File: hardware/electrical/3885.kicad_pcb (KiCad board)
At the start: 4 copper layers, 33 x 77 mm, 9 parts, among them J1 USB_B_Micro, J4 JST-PH, J5 FFC, SW2 EVQP7C01K

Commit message: Component placement
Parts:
- added C1: 10u, Capacitor_SMD:C_0402_1005Metric, F.Cu at (146.7, 137.5)
- added C10: 100n, Capacitor_SMD:C_0402_1005Metric, F.Cu at (141.0, 116.0)
- added C11: 12p, Capacitor_SMD:C_0603_1608Metric, F.Cu at (137.8, 116.5)
- added C12: 100n, Capacitor_SMD:C_0402_1005Metric, F.Cu at (141.0, 120.0)
- added C13: 100n, Capacitor_SMD:C_0402_1005Metric, F.Cu at (146.0, 127.0)
- added C14: 12p, Capacitor_SMD:C_0603_1608Metric, F.Cu at (137.8, 119.5)
- added C15: 100n, Capacitor_SMD:C_0402_1005Metric, F.Cu at (156.8, 127.0)
- added C16: 100n, Capacitor_SMD:C_0402_1005Metric, F.Cu at (161.0, 111.0)
- added C17: 100n, Capacitor_SMD:C_0402_1005Metric, F.Cu at (145.0, 106.5)
- added C18: 100n, Capacitor_SMD:C_0402_1005Metric, F.Cu at (141.0, 114.9)
- added C2: 100n, Capacitor_SMD:C_0402_1005Metric, F.Cu at (140.8, 137.8)
- added C20: 2u2, Capacitor_SMD:C_0402_1005Metric, F.Cu at (155.5, 127.0)
- added C22: 2u2, Capacitor_SMD:C_0402_1005Metric, F.Cu at (161.0, 112.0)
- added C25: 4u7, Capacitor_SMD:C_0402_1005Metric, F.Cu at (141.0, 109.8)
- added C27: 100n, Capacitor_SMD:C_0402_1005Metric, F.Cu at (141.0, 113.8)
- added C29: 100n, Capacitor_SMD:C_0402_1005Metric, F.Cu at (141.0, 121.5)
- added C3: 100n, Capacitor_SMD:C_0402_1005Metric, F.Cu at (144.8, 131.2)
- added C31: 1u, Capacitor_SMD:C_0402_1005Metric, F.Cu at (141.0, 122.5)
- added C32: 15p, Capacitor_SMD:C_0603_1608Metric, F.Cu at (137.8, 110.2)
- added C33: 15p, Capacitor_SMD:C_0603_1608Metric, F.Cu at (137.8, 113.3)
- added C34: 1u, Capacitor_SMD:C_0402_1005Metric, F.Cu at (141.0, 123.5)
- added C35: 4u7, Capacitor_SMD:C_0402_1005Metric, F.Cu at (156.6, 89.3)
- added C36: 100n, Capacitor_SMD:C_0402_1005Metric, F.Cu at (154.8, 89.3)
- added C37: 10u, Capacitor_SMD:C_0402_1005Metric, F.Cu at (160.5, 118.8)
- added C38: 10u, Capacitor_SMD:C_0402_1005Metric, F.Cu at (161.0, 113.0)
- added C39: 100n, Capacitor_SMD:C_0402_1005Metric, F.Cu at (159.2, 128.5)
- added C4: 100n, Capacitor_SMD:C_0402_1005Metric, F.Cu at (135.2, 131.2)
- added C40: 100n, Capacitor_SMD:C_0402_1005Metric, F.Cu at (148.5, 127.0)
- added C42: 4u7, Capacitor_SMD:C_0402_1005Metric, F.Cu at (155.5, 136.0)
- added C43: 4u7, Capacitor_SMD:C_0402_1005Metric, F.Cu at (154.2, 130.7)
- added C44: 100n, Capacitor_SMD:C_0402_1005Metric, F.Cu at (149.0, 75.7)
- added C45: 15p, Capacitor_SMD:C_0603_1608Metric, F.Cu at (146.2, 76.0)
- added C46: 1u, Capacitor_SMD:C_0402_1005Metric, F.Cu at (161.8, 79.8)
- added C47: 1u, Capacitor_SMD:C_0402_1005Metric, F.Cu at (157.2, 79.8)
- added C48: 1u, Capacitor_SMD:C_0402_1005Metric, F.Cu at (161.8, 73.3)
- added C49: 1u, Capacitor_SMD:C_0402_1005Metric, F.Cu at (157.2, 73.3)
- added C5: 100n, Capacitor_SMD:C_0402_1005Metric, F.Cu at (135.2, 133.8)
- added C52: 100n, Capacitor_SMD:C_0402_1005Metric, F.Cu at (153.0, 75.8)
- added C53: 100n, Capacitor_SMD:C_0402_1005Metric, F.Cu at (150.0, 75.7)
- added C54: 100n, Capacitor_SMD:C_0402_1005Metric, F.Cu at (138.3, 73.5)
- added C6: 4u7, Capacitor_SMD:C_0402_1005Metric, F.Cu at (139.5, 137.8)
- added C7: 4u7, Capacitor_SMD:C_0402_1005Metric, F.Cu at (135.2, 132.5)
- added C8: 4u7, Capacitor_SMD:C_0402_1005Metric, F.Cu at (144.8, 132.5)
- added C9: 4u7, Capacitor_SMD:C_0402_1005Metric, F.Cu at (144.8, 127.0)
- added D1: SMF6.0CA, Diode_SMD:D_SOD-123F, F.Cu at (150.0, 136.8)
- added D4: D_Schottky, Diode_SMD:D_SOD-323, F.Cu at (157.8, 135.2)
- added FB1: 600R, Inductor_SMD:L_0805_2012Metric, F.Cu at (150.4, 134.6)
- added J2: TC2030, Connector:Tag-Connect_TC2030-IDC-FP_2x03_P1.27mm_Vertical, F.Cu at (160.7, 94.6)
- added J3: Micro_SD_Card_Det1, 3885:microSD_HC_XKB_XKTF-N02-N, F.Cu at (142.8, 91.5)
- added JP1: Jumper_2_Open, Jumper:SolderJumper-2_P1.3mm_Open_Pad1.0x1.5mm, F.Cu at (149.8, 105.8)
- added JP3: SolderJumper_3_Bridged12, Jumper:SolderJumper-3_P1.3mm_Bridged12_Pad1.0x1.5mm, F.Cu at (148.2, 80.8)
- added Q1: AO3400A, Package_TO_SOT_SMD:SOT-23, F.Cu at (162.0, 125.5)
- added Q2: AO3400A, Package_TO_SOT_SMD:SOT-23, F.Cu at (162.0, 122.0)
- added Q3: AO3401A, Package_TO_SOT_SMD:SOT-23, F.Cu at (161.0, 132.8)
- added Q4: AO3401A, Package_TO_SOT_SMD:SOT-23, F.Cu at (161.0, 136.2)
- added Q5: 2N7002, Package_TO_SOT_SMD:SOT-23, F.Cu at (148.0, 131.2)
- added Q6: AO3401A, Package_TO_SOT_SMD:SOT-23, F.Cu at (151.5, 131.2)
- added Q7: AO3401A, Package_TO_SOT_SMD:SOT-23, F.Cu at (159.5, 76.2)
- added Q8: 2N7002, Package_TO_SOT_SMD:SOT-23, F.Cu at (156.2, 139.6)
- added R1: 680R, Resistor_SMD:R_0402_1005Metric, F.Cu at (138.2, 137.8)
- added R10: 10k, Resistor_SMD:R_0402_1005Metric, F.Cu at (142.3, 138.5)
- added R11: 68R, Resistor_SMD:R_0603_1608Metric, F.Cu at (159.0, 139.9)
- added R12: 10k, Resistor_SMD:R_0402_1005Metric, F.Cu at (142.3, 139.6)
- added R13: 10k, Resistor_SMD:R_0402_1005Metric, F.Cu at (155.3, 93.8)
- added R14: 10k, Resistor_SMD:R_0402_1005Metric, F.Cu at (155.3, 92.7)
- added R15: 10k, Resistor_SMD:R_0402_1005Metric, F.Cu at (155.3, 91.5)
- added R16: 10k, Resistor_SMD:R_0402_1005Metric, F.Cu at (155.3, 87.2)
- added R17: 10k, Resistor_SMD:R_0402_1005Metric, F.Cu at (155.3, 86.0)
- added R18: 10k, Resistor_SMD:R_0402_1005Metric, F.Cu at (155.3, 85.0)
- added R19: 1k8, Resistor_SMD:R_0603_1608Metric, F.Cu at (162.5, 118.6)
- added R2: 12k±1%, Resistor_SMD:R_0402_1005Metric, F.Cu at (135.2, 135.0)
- added R20: 10k, Resistor_SMD:R_0402_1005Metric, F.Cu at (141.0, 108.8)
- added R21: 100R, Resistor_SMD:R_0402_1005Metric, F.Cu at (155.5, 137.0)
- added R22: 2k7, Resistor_SMD:R_0603_1608Metric, F.Cu at (158.2, 130.2)
- added R23: 330, Resistor_SMD:R_0402_1005Metric, F.Cu at (163.5, 132.2)
- added R24: 1k, Resistor_SMD:R_0402_1005Metric, F.Cu at (159.2, 126.5)
- added R25: 1k, Resistor_SMD:R_0402_1005Metric, F.Cu at (158.2, 132.2)
- added R26: 10k, Resistor_SMD:R_0402_1005Metric, F.Cu at (154.2, 129.0)
- added R27: 10k, Resistor_SMD:R_0402_1005Metric, F.Cu at (148.0, 128.5)
- added R28: 1k, Resistor_SMD:R_0402_1005Metric, F.Cu at (151.0, 75.8)
- added R29: 10k, Resistor_SMD:R_0402_1005Metric, F.Cu at (162.2, 76.2)
- added R3: 33R, Resistor_SMD:R_0402_1005Metric, F.Cu at (144.8, 133.8)
- added R30: 4k7, Resistor_SMD:R_0402_1005Metric, F.Cu at (154.0, 75.8)
- added R31: 4k7, Resistor_SMD:R_0402_1005Metric, F.Cu at (152.0, 75.8)
- added R32: 6k8, Resistor_SMD:R_0402_1005Metric, F.Cu at (141.0, 125.5)
- added R33: 10k, Resistor_SMD:R_0402_1005Metric, F.Cu at (141.0, 124.5)
- added R4: 0R, Resistor_SMD:R_0603_1608Metric_Pad0.98x0.95mm_HandSolder, F.Cu at (140.2, 117.2)
- added R5: 0R, Resistor_SMD:R_0603_1608Metric_Pad0.98x0.95mm_HandSolder, F.Cu at (140.2, 118.8)
- added R6: 33R, Resistor_SMD:R_0402_1005Metric, F.Cu at (141.6, 105.1)
- added R7: 10k, Resistor_SMD:R_0402_1005Metric, F.Cu at (148.0, 106.5)
- added R8: 0R, Resistor_SMD:R_0603_1608Metric_Pad0.98x0.95mm_HandSolder, F.Cu at (140.2, 111.0)
- added R9: 0R, Resistor_SMD:R_0603_1608Metric_Pad0.98x0.95mm_HandSolder, F.Cu at (140.2, 112.5)
- added SW1: TS-1187A-B-A-B, 3885:SW_SPST_XKB_TS-1187A, F.Cu at (136.8, 103.8)
- added U1: USB3300-EZK, Package_DFN_QFN:QFN-32-1EP_5x5mm_P0.5mm_EP3.45x3.45mm, F.Cu at (140.0, 133.0)
- added U2: TP4054, Package_TO_SOT_SMD:SOT-23-5, F.Cu at (161.8, 115.8)
- added U3: TLV70028DCKR, Package_TO_SOT_SMD:SOT-353_SC-70-5, F.Cu at (159.5, 79.5)
- added U4: WL2803E33-5/TR, Package_TO_SOT_SMD:SOT-23-5, F.Cu at (155.0, 133.2)
- added U5: AP9101CK6-AYTRG1, Package_TO_SOT_SMD:SOT-23-6, F.Cu at (162.0, 129.0)
- added U6: APX803S-31SA-7, Package_TO_SOT_SMD:SOT-23, F.Cu at (151.2, 127.5)
- added U8: STM32F446VET6, Package_QFP:LQFP-100_14x14mm_P0.5mm, F.Cu at (151.0, 117.0)
- added U9: TLV70012DCKR, Package_TO_SOT_SMD:SOT-353_SC-70-5, F.Cu at (159.5, 73.0)
- added X2: SG-8018CA 24.0000M-TJHPA3r, Oscillator:Oscillator_SMD_SeikoEpson_SG8002CA-4Pin_7.0x5.0mm_HandSoldering, F.Cu at (137.4, 78.1)
- added Y1: 24MHz, Crystal:Crystal_SMD_SeikoEpson_TSX3225-4Pin_3.2x2.5mm, F.Cu at (135.0, 117.2)
- added Y2: 32.768kHz, Crystal:Crystal_SMD_3215-2Pin_3.2x1.5mm, F.Cu at (135.8, 111.8)
- moved J4 5.60 mm to (162.2, 107.3)
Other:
- outline, holes or cut-outs redrawn

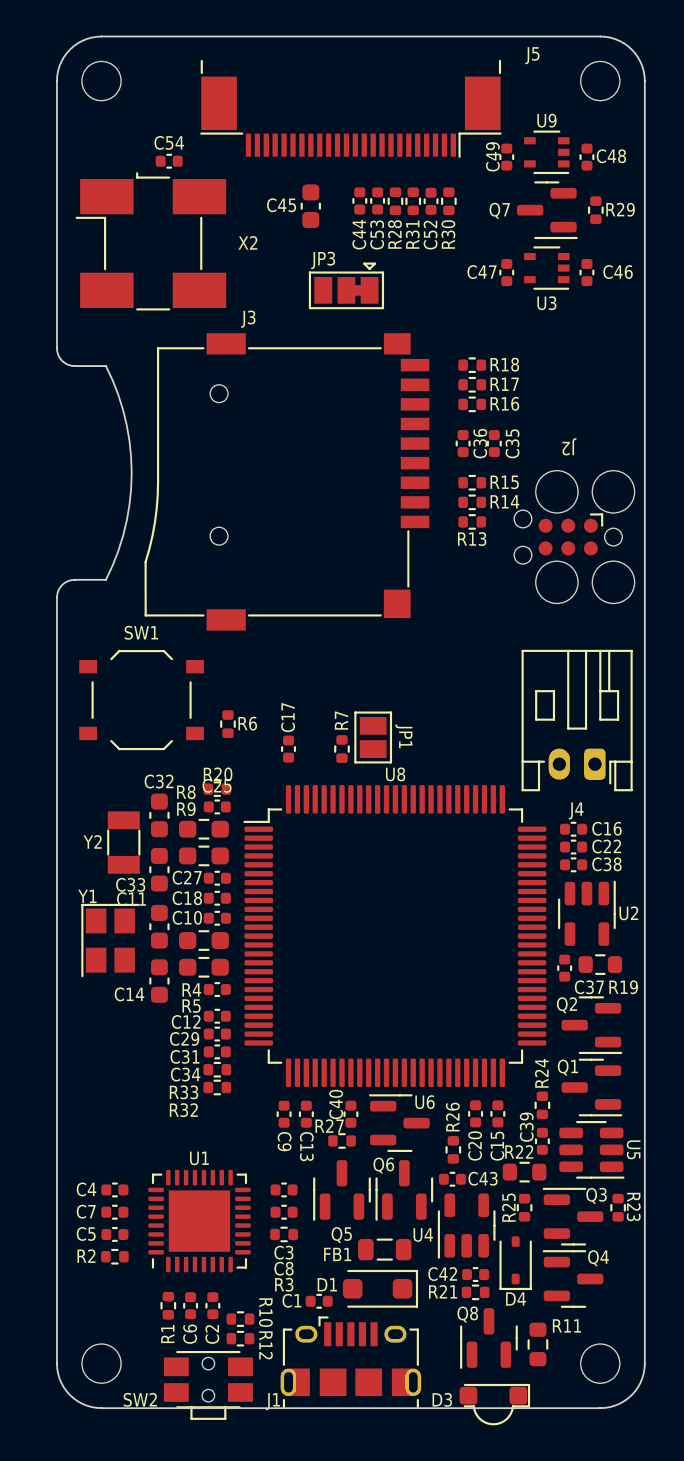
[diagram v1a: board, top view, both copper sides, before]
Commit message: Route ULPI and power supply
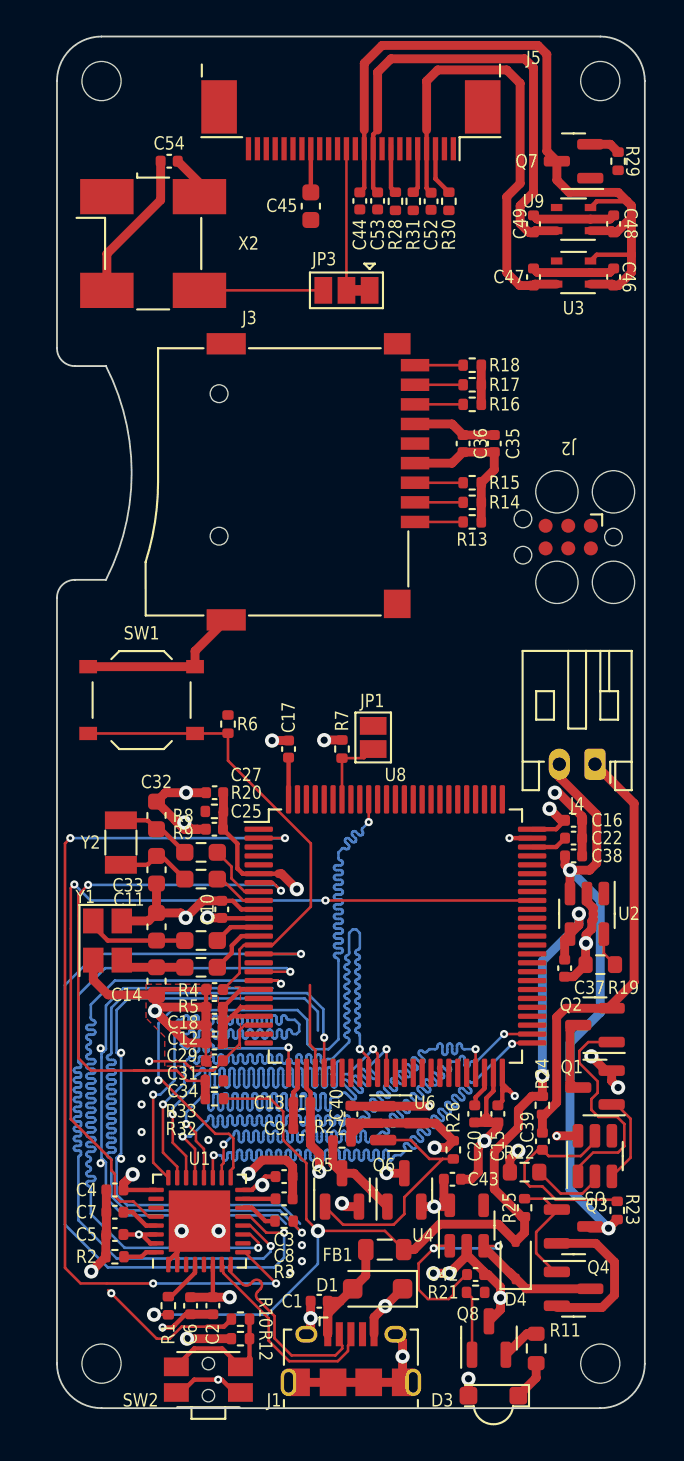
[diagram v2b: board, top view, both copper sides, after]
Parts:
- moved C18 5.13 mm to (140.8, 120.0)
- moved C27 4.80 mm to (140.8, 109.0)
- moved C48 4.04 mm to (163.2, 77.0)
- moved C49 4.04 mm to (158.8, 77.0)
- moved U9 4.04 mm to (161.0, 76.8)
- moved Q7 3.13 mm to (161.0, 73.5)
- moved R29 3.02 mm to (163.5, 73.5)
- moved C46 1.52 mm to (163.2, 80.0)
- moved C47 1.52 mm to (158.8, 80.0)
- moved U3 1.52 mm to (161.0, 79.8)
- moved R8 1.31 mm to (140.1, 112.3)
- moved R9 1.31 mm to (140.1, 113.8)
- moved C9 1.28 mm to (145.8, 127.8), turned to 180 degrees
- moved C25 1.26 mm to (140.8, 111.0), turned to 180 degrees
- moved R20 1.26 mm to (140.8, 110.0), turned to 180 degrees
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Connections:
- U1 pad 31: +3V3 -> VDD
- U8 pad 2: unconnected-(U8-PE3-Pad2) -> USB_OTG_HS_RESET
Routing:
- net GND: track 0.00 -> 220.7 mm, vias 0 -> 40
- net VBUS: track 0.00 -> 61.5 mm, vias 0 -> 4
- net VDD: track 0.00 -> 60.7 mm, vias 0 -> 11
- net USB_OTG_HS_RESET: track 0.00 -> 52.6 mm, vias 0 -> 4
- net USB_OTG_HS_ULPI_D0: track 0.00 -> 49.5 mm, vias 0 -> 2
- net RCC_MCO_1: track 0.00 -> 47.5 mm, vias 0 -> 2
- net USB_OTG_HS_ULPI_STP: track 0.00 -> 47.4 mm, vias 0 -> 2
- net USB_OTG_HS_ULPI_DIR: track 0.00 -> 46.8 mm, vias 0 -> 2
- net USB_OTG_HS_ULPI_CLK: track 0.00 -> 46.8 mm, vias 0 -> 2
- net USB_OTG_HS_ULPI_D7: track 0.00 -> 46.7 mm, vias 0 -> 2
- net USB_OTG_HS_ULPI_D4: track 0.00 -> 46.6 mm, vias 0 -> 2
- net USB_OTG_HS_ULPI_D2: track 0.00 -> 46.6 mm, vias 0 -> 2
- net USB_OTG_HS_ULPI_NXT: track 0.00 -> 46.6 mm, vias 0 -> 2
- net USB_OTG_HS_ULPI_D6: track 0.00 -> 46.4 mm, vias 0 -> 2
- net USB_OTG_HS_ULPI_D3: track 0.00 -> 46.4 mm, vias 0 -> 2
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- added copper zone on F.Cu, net GND
- added copper zone on In2.Cu, net GND
- added copper zone on F.Cu, net VDD
- added copper zone on In1.Cu, net VDD

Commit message: Revise power supply
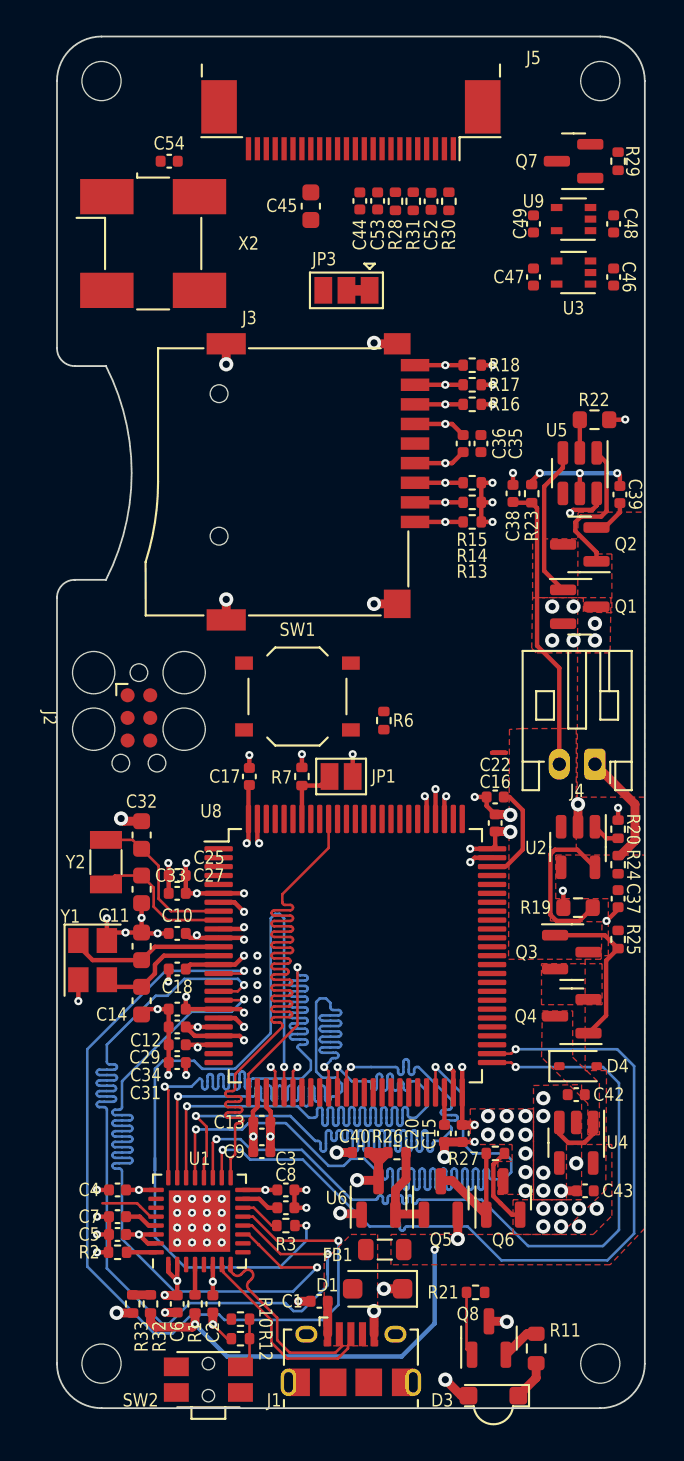
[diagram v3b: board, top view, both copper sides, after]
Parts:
- removed R4, R5, R8, R9: 0R, Resistor_SMD:R_0603_1608Metric_Pad0.98x0.95mm_HandSolder
- moved R22 42.4 mm to (162.2, 88.0), turned to 0 degrees
- moved R23 40.5 mm to (158.7, 92.2)
- moved U5 38.3 mm to (161.3, 91.0), turned to -90 degrees
- moved C39 36.6 mm to (163.6, 92.2), turned to 90 degrees
- moved Q1 27.0 mm to (161.3, 98.5), turned to 0 degrees
- moved Q2 27.0 mm to (161.3, 95.0)
- moved J2 26.2 mm to (136.6, 104.8), turned to -90 degrees
- moved R20 22.7 mm to (163.5, 111.0), turned to -90 degrees
- moved C38 20.6 mm to (157.6, 92.2), turned to -90 degrees
- moved R25 15.9 mm to (163.5, 117.2), turned to 90 degrees
- moved Q3 15.4 mm to (160.9, 117.9)
- moved Q4 15.3 mm to (160.9, 121.5), turned to 180 degrees
- moved R24 14.2 mm to (163.5, 113.0), turned to -90 degrees
- moved R33 13.3 mm to (136.2, 137.7), turned to -90 degrees
- moved R32 12.1 mm to (137.2, 137.7), turned to 90 degrees
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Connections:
- C11 pad 2: Net-(C11-Pad2) -> /Microcontroller/RCC_OSC_IN
- C14 pad 1: Net-(C14-Pad1) -> /Microcontroller/RCC_OSC_OUT
- C32 pad 1: Net-(C32-Pad1) -> /Microcontroller/RCC_OSC32_IN
- C33 pad 1: Net-(C33-Pad1) -> /Microcontroller/RCC_OSC32_OUT
- R20 pad 1: +3V3 -> VDD
- U8 pad 2: USB_OTG_HS_RESET -> unconnected-(U8-PE3-Pad2)
- Y1 pad 1: Net-(C11-Pad2) -> /Microcontroller/RCC_OSC_IN
- Y1 pad 3: Net-(C14-Pad1) -> /Microcontroller/RCC_OSC_OUT
- Y2 pad 1: Net-(C33-Pad1) -> /Microcontroller/RCC_OSC32_OUT
- Y2 pad 2: Net-(C32-Pad1) -> /Microcontroller/RCC_OSC32_IN
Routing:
- net GND: track 220.7 -> 71.8 mm, vias 40 -> 80
- net USB_OTG_HS_RESET: track 52.6 -> 0.00 mm, vias 4 -> 0
- net RCC_MCO_1: track 47.5 -> 3.32 mm, vias 2 -> 0
- net /Camera Module/DOVDD: track 44.0 -> 0.00 mm
- net VBUS: track 61.5 -> 22.9 mm, vias 4 -> 2
- net /Microcontroller/SYS_WKUP1: track 31.6 -> 2.65 mm, vias 2 -> 1
- net /Microcontroller/SYS_WKUP0: track 30.3 -> 2.00 mm, vias 2 -> 1
- net /Camera Module/DVDD: track 27.6 -> 0.00 mm
- net /Camera Module/AVDD: track 26.3 -> 0.00 mm
- net Net-(U8-NRST): track 27.1 -> 3.58 mm, vias 0 -> 1
- net +BATT: track 34.4 -> 16.4 mm, vias 2 -> 0
- net +3V3: track 43.1 -> 25.5 mm, vias 3 -> 12
- net -BATT: track 25.4 -> 8.97 mm
- net Net-(#FLG07-pwr): track 19.4 -> 3.63 mm, vias 2 -> 0
- net VDD: track 60.7 -> 49.0 mm, vias 11 -> 37
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- added copper zone on F.Cu, net +3V3
- added copper zone on In1.Cu, net +3V3
- added copper zone on F.Cu, net +BATT
- added copper zone on F.Cu, net -BATT
- added copper zone on F.Cu, net Net-(#FLG07-pwr)
- added copper zone on F.Cu, net Net-(D1-A2)
- added copper zone on F.Cu, net Net-(Q1-D)
- added copper zone on F.Cu, net Net-(Q3-S)
- added copper zone on F.Cu, net VBUS

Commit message: Remove components from in front of the JST connector
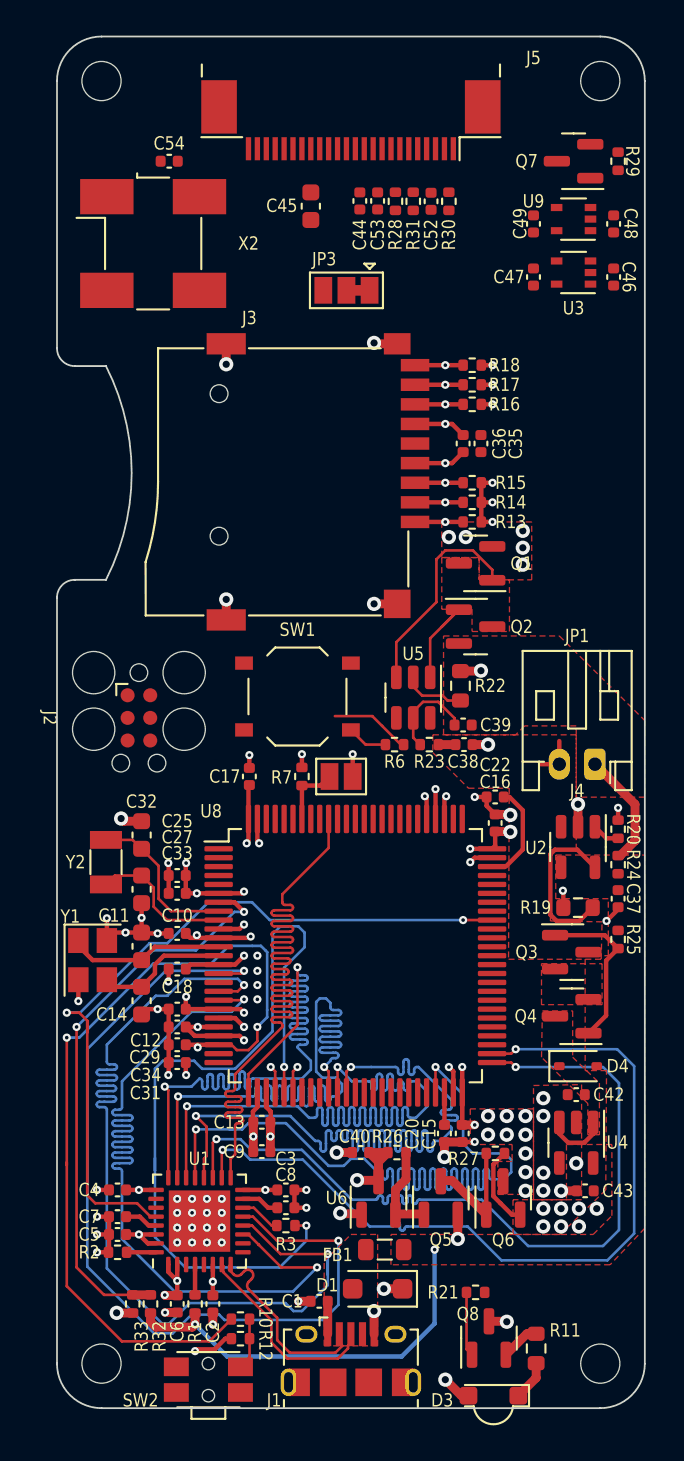
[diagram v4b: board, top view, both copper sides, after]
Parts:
- moved R22 16.7 mm to (154.7, 103.0), turned to 90 degrees
- moved U5 15.7 mm to (152.0, 103.6)
- moved C39 15.6 mm to (154.8, 105.2), turned to 180 degrees
- moved R23 15.2 mm to (152.9, 106.2), turned to 0 degrees
- moved C38 14.4 mm to (154.8, 106.2), turned to 180 degrees
- moved Q2 7.45 mm to (155.5, 99.6), turned to 0 degrees
- moved Q1 6.34 mm to (155.5, 96.1), turned to 180 degrees
- moved R6 1.48 mm to (150.9, 106.2), turned to 180 degrees
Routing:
- net /Microcontroller/SYS_WKUP0: track 2.00 -> 48.4 mm, vias 1 -> 3
- net RCC_MCO_1: track 3.32 -> 43.0 mm, vias 0 -> 2
- net /Microcontroller/SYS_WKUP1: track 2.65 -> 32.0 mm, vias 1 -> 2
- net +BATT: track 16.4 -> 3.31 mm
- net NRST: track 0.00 -> 4.52 mm
- net Net-(Q1-G): track 8.56 -> 12.4 mm
- net -BATT: track 8.97 -> 6.53 mm
- net Net-(U8-NRST): track 3.58 -> 5.86 mm
- net Net-(Q2-G): track 8.20 -> 6.01 mm
- net Net-(U5-VM): track 1.86 -> 3.50 mm
- net Net-(U8-VCAP_2): track 6.48 -> 4.94 mm
- net Net-(#FLG03-pwr): track 7.10 -> 5.66 mm, vias 3 -> 0
- net GND: track 71.8 -> 70.9 mm
- net (no net): vias 1 -> 0

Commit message: PCB Rev 2.0
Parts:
- moved C17 0.78 mm to (143.3, 108.7), turned to 0 degrees
- moved J2 0.26 mm to (136.9, 104.8)
- moved JP1 0.24 mm to (147.9, 107.8)
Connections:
- net /Microcontroller/SYS_JTCK-SWCLK renamed SYS_JTCK-SWCLK
- net /Microcontroller/SYS_JTDO-SWO renamed SYS_JTDO-SWO
- net /Microcontroller/SYS_JTMS-SWDIO renamed SYS_JTMS-SWDIO
- U8 pad 34: unconnected-(U8-PC5-Pad34) -> USB_OTG_HS_RESET
- U8 pad 45: unconnected-(U8-PE14-Pad45) -> STAT
- U8 pad 61: unconnected-(U8-PD14-Pad61) -> CHARGE_STAT
- U8 pad 62: unconnected-(U8-PD15-Pad62) -> Cam_Enable
- U8 pad 82: unconnected-(U8-PD1-Pad82) -> SD_DETECT
- U8 pad 88: unconnected-(U8-PD7-Pad88) -> Cam_PWDN
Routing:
- net Cam_Enable: track 0.00 -> 84.2 mm, vias 0 -> 4
- net DCMI_D7: track 0.00 -> 67.9 mm, vias 0 -> 2
- net DCMI_PIXCLK: track 1.53 -> 69.2 mm, vias 1 -> 2
- net DCMI_D0: track 0.00 -> 67.3 mm, vias 0 -> 2
- net DCMI_D1: track 0.00 -> 66.5 mm, vias 0 -> 2
- net DCMI_D5: track 0.00 -> 65.4 mm, vias 0 -> 2
- net DCMI_VSYNC: track 0.00 -> 65.1 mm, vias 0 -> 2
- net DCMI_D6: track 0.00 -> 64.9 mm, vias 0 -> 2
- net DCMI_D4: track 0.00 -> 64.8 mm, vias 0 -> 2
- net DCMI_D3: track 0.00 -> 64.8 mm, vias 0 -> 2
- net DCMI_D2: track 0.00 -> 64.6 mm, vias 0 -> 2
- net DCMI_HSYNC: track 1.53 -> 65.3 mm, vias 1 -> 2
- net Cam_SDA: track 0.00 -> 56.4 mm, vias 0 -> 2
- net Cam_SCL: track 0.00 -> 55.8 mm, vias 0 -> 2
- net GND: track 70.9 -> 115.4 mm, vias 80 -> 457
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- added copper zone on F.Cu, net /Camera Module/DOVDD
- added copper zone on B.Cu, net GND
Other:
- board text added: "ELEC3885 GDP Group 4 - BikeCam"
- board text added: "Main PCB Rev 2.0"
- board text added: "{ "ViaStitching": "0.1", "stitch_zone_0": { "HSpacing": "1", "VSpacing": "1", "Clearance": "0", "Randomize": false } }"
- board text added: "© Frank Plowman 2023"
